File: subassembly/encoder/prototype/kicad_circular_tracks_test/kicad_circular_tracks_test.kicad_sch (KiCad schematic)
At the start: 34 parts, among them J1 Conn_01x05, J2 Conn_01x05, U1 ATSAMD10D13A-M

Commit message: SOICbite connector, RC filters for inputs
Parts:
- added C3, C4, C5, C6: 0.1uF, Capacitor_SMD:C_0603_1608Metric, symbol Device:C_Small
- added J3: SOICbite-SWD, BVH_SOICbite:SOICbite_renumbered, symbol BVH_SOICbite:SOICbite-SWD
- added R10, R11, R9: 1k, Resistor_SMD:R_0603_1608Metric, symbol Device:R_Small
- added R12: 10k, Resistor_SMD:R_0603_1608Metric, symbol Device:R_Small
- added R7, R8: 2k2, Resistor_SMD:R_0603_1608Metric, symbol Device:R_Small
- U1: footprint Package_DFN_QFN:QFN-24-1EP_4x4mm_P0.5mm_EP2.6x2.6mm_ThermalVias -> Package_DFN_QFN:QFN-24-1EP_4x4mm_P0.5mm_EP2.6x2.6mm
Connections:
- net ENC_A: now also C3.1, R9.2; no longer S1.3 (A)
- net ENC_B: now also C4.1, R10.2; no longer S1.5 (B)
- net ENC_SW: now also C5.1, R11.2; no longer S1.1 (SW1)
- net GND: now also C3.2, C4.2, C5.2, C6.2, J3.7 (GND)
- net I2C_SCL: now also J3.3, R7.2
- net I2C_SDA: now also J3.5, R8.2
- net SWCLK: now also J3.4 (SWCLK)
- net SWDIO: now also J3.8 (SWDIO)
- net +3V3 renamed +3.3V
- net +3.3V: now also J3.1 (Vcc), R12.1, R7.1, R8.1
- net ~RESET renamed ~{RESET}
- net ~{RESET}: now also C6.1, J3.2 (NRST), R12.2
- new net ENC_A_RAW: R9.1, S1.3 (A)
- new net ENC_B_RAW: R10.1, S1.5 (B)
- new net ENC_SW_RAW: R11.1, S1.1 (SW1)
- no-connect marks 0 -> 9
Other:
- note added: "1k PU on SWCLK from SAMD10 DS 36.7"
- note added: "Always populate resistors with at least 0 ohm. Populate filter capacitors as needed. 0.1ms Filter: R - 1k C - 0.1uF"
- note added: "Charlieplexed LED circle"
- note added: "Column annode Row cathode"
- note added: "Duplicate 0.1" header until SOICbite proves reliable"
- note added: "I2C Pull Ups"
- note added: "Populate for last module in chain"
- note added: "Rotary encoder and debounce networks"
- note added: "SWD Connections"
- moved on the sheet: C1, C2, D1, D10, D11, D12, D13, D14, D15, D16, D17, D18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

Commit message: WIP
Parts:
- removed J2: Conn_01x05, Connector_PinSocket_2.54mm:PinSocket_1x05_P2.54mm_Vertical, symbol Connector_Generic:Conn_01x05
- added J4: Conn_01x05, Connector_PinSocket_1.27mm:PinSocket_1x05_P1.27mm_Vertical, symbol Connector_Generic:Conn_01x05
- added R13, R14: ?, Resistor_SMD:R_0603_1608Metric, symbol Device:R_Small
- J1: footprint Connector_PinSocket_2.54mm:PinSocket_1x05_P2.54mm_Vertical -> Connector_PinSocket_1.27mm:PinSocket_1x05_P1.27mm_Vertical
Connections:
- net +3.3V: now also J4.2 (Pin_2), R13.1
- net A: now also U1.2 (PA03); no longer U1.1 (PA02)
- net B: now also U1.3 (PA04); no longer U1.2 (PA03)
- net C: now also U1.6 (PA07); no longer U1.5 (PA06)
- net D: now also U1.5 (PA06); no longer U1.4 (PA05)
- net E: now also U1.4 (PA05); no longer U1.3 (PA04)
- net GND: now also J4.1 (Pin_1), R14.2
- net I2C_SCL: now also J4.3 (Pin_3)
- net I2C_SDA: now also J4.4 (Pin_4)
- net INT: now also J4.5 (Pin_5)
- new net ADDR_SET: R13.2, R14.1, U1.1 (PA02)
- no-connect marks 9 -> 8
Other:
- note added: "See firmware documentation for valid values"
- note added: "Voltage divider to ADC to allow I2C address configuration at boot."
- note removed: "Duplicate 0.1" header until SOICbite proves reliable"
- moved on the sheet: C6, R12, R6

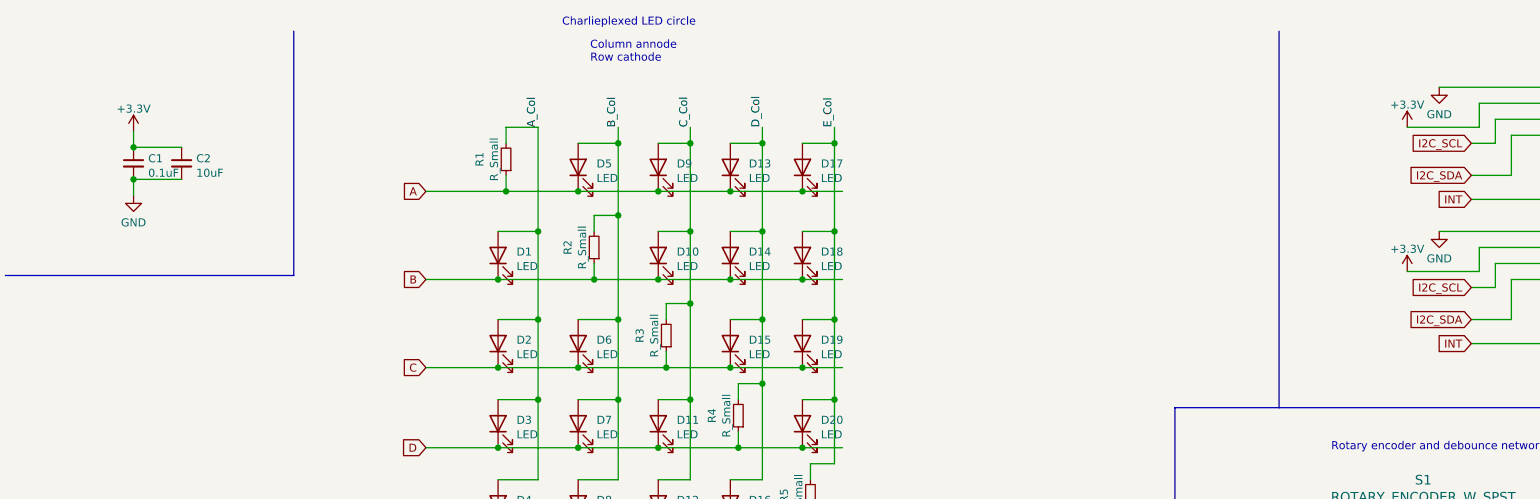
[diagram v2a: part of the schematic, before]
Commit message: Keyboard matrix prototype + encoder update
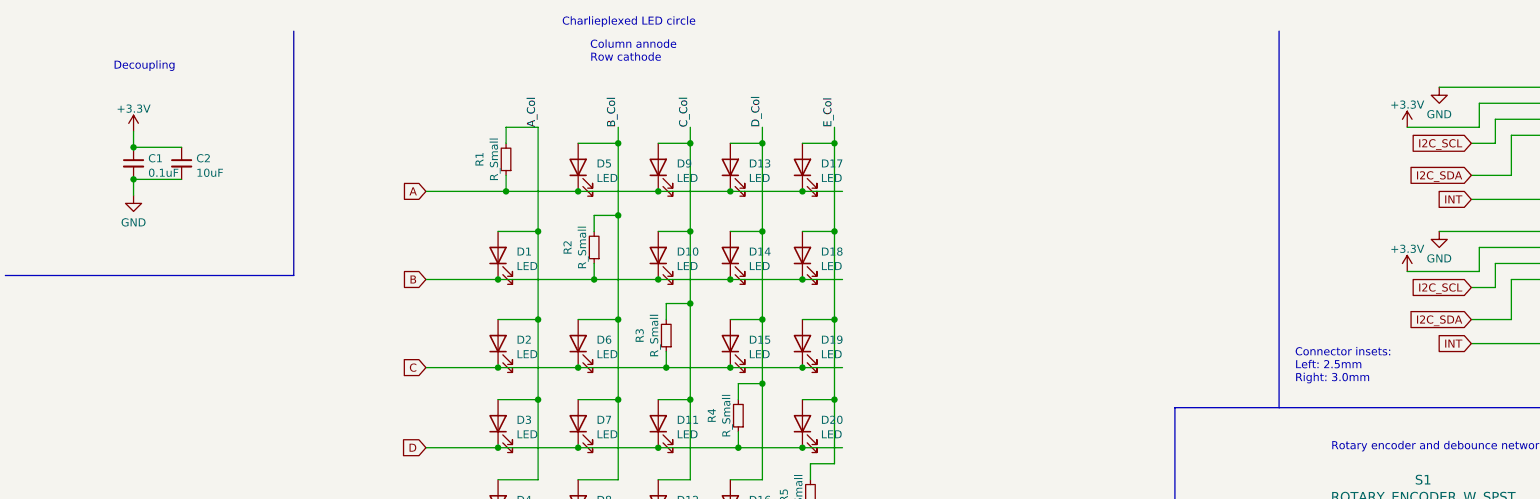
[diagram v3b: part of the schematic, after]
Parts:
- U1: symbol MCU_Microchip_SAMD:ATSAMD10D13A-M -> BVH_MCU_Microchip-SAMD:ATSAMD10D13A-M
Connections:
- net GND: now also U1.25 (GND)
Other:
- note added: "Connector insets: Left: 2.5mm Right: 3.0mm"
- note added: "Decoupling"
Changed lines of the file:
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@@
     (effects (font (size 1.27 1.27)) (justify left bottom))
   )
+  (text "Decoupling" (at 30.48 19.05 0)
+    (effects (font (size 1.27 1.27)) (justify left bottom))
+  )
   (text "Charlieplexed LED circle" (at 101.6 12.065 0)
+    (effects (font (size 1.27 1.27)) (justify left bottom))
+  )
+  (text "Connector insets:\nLeft: 2.5mm\nRight: 3.0mm" (at 217.805 68.58 0)
     (effects (font (size 1.27 1.27)) (justify left bottom))
   )
@@
     (pin "5")
   )
-  (symbol (lib_id "MCU_Microchip_SAMD:ATSAMD10D13A-M") (at 59.69 153.67 0) (unit 1)
+  (symbol (lib_id "BVH_MCU_Microchip-SAMD:ATSAMD10D13A-M") (at 59.69 153.67 0) (unit 1)
     (in_bom yes) (on_board yes)
     (property "Reference" "U1" (id 0) (at 59.69 124.5828 0))
@@
     (pin "23")
     (pin "24")
+    (pin "25")
     (pin "3")
     (pin "4")
